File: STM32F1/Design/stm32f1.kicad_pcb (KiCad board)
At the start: 2 copper layers, 31 parts, among them J1 USB_C_Receptacle_USB2.0, J2 Conn_01x04_Pin, J3 Conn_01x04_Pin, J4 Conn_01x04_Pin, SW1 SW_SPDT, U1 STM32F103C8Tx, U2 AMS1117-3.3, Y1 16MHz

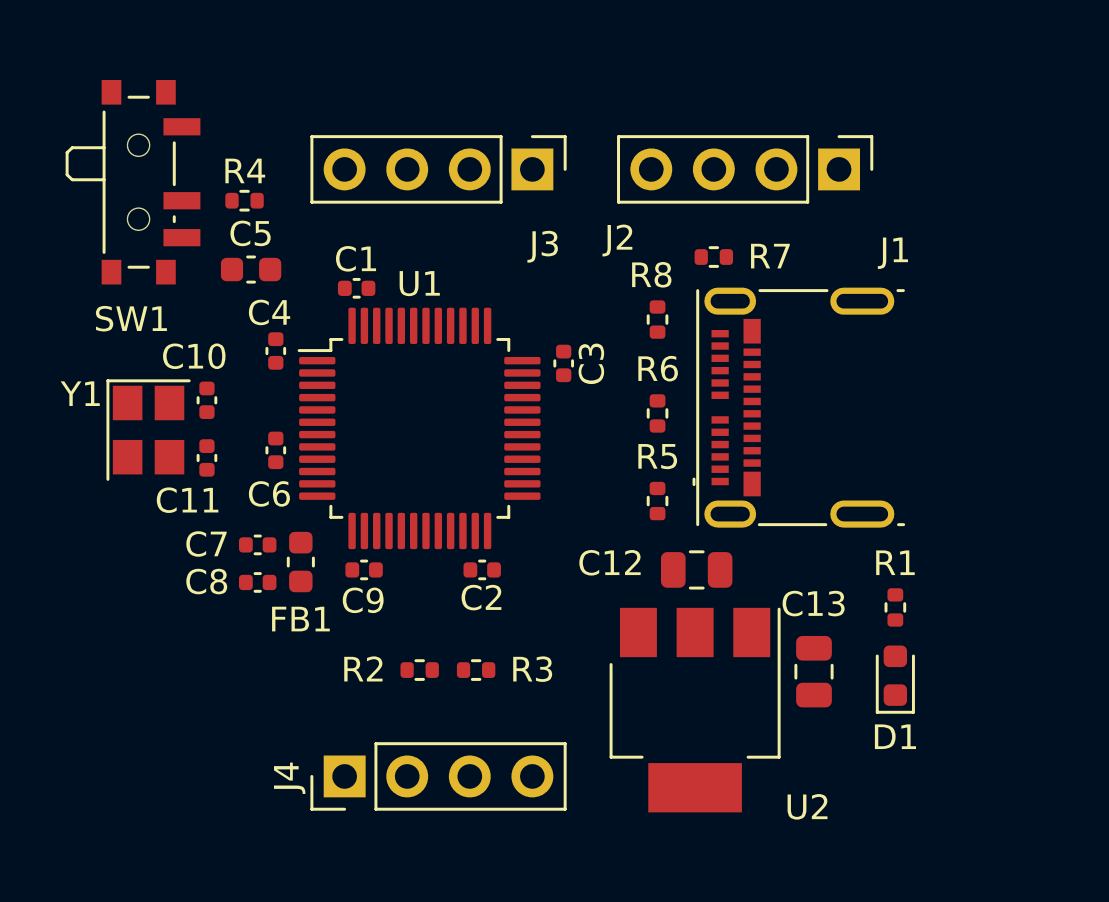
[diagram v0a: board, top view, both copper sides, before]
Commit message: Fine tunes PCB layout and added borders, Started routing
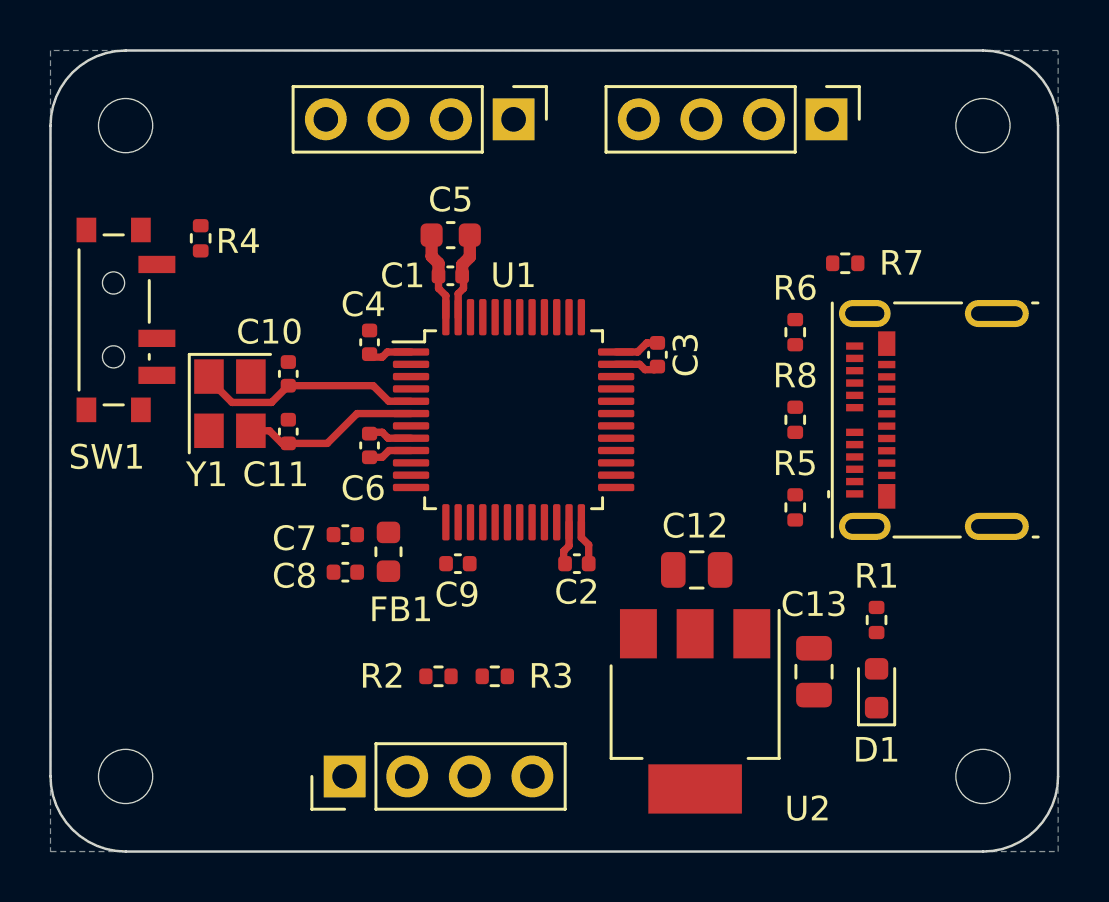
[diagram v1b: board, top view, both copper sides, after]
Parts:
- added H1: MountingHole, MountingHole:MountingHole_2.2mm_M2, F.Cu at (73.4, 55.4)
- added H2: MountingHole, MountingHole:MountingHole_2.2mm_M2, F.Cu at (73.4, 81.8)
- added H3: MountingHole, MountingHole:MountingHole_2.2mm_M2, F.Cu at (38.6, 55.4)
- added H4: MountingHole, MountingHole:MountingHole_2.2mm_M2, F.Cu at (38.6, 81.8)
- moved C5 8.22 mm to (51.8, 59.8)
- moved R8 6.91 mm to (65.8, 67.3), turned to -90 degrees
- moved R6 6.49 mm to (65.8, 63.8)
- moved SW1 5.68 mm to (38.4, 63.3)
- moved R5 5.59 mm to (65.8, 70.9)
- moved J1 5.49 mm to (71.4, 67.3)
- moved R7 5.34 mm to (67.8, 61.0)
- moved C2 3.85 mm to (56.9, 73.2)
- moved C1 3.84 mm to (51.8, 61.5)
- moved C3 3.82 mm to (60.2, 64.7)
- moved U1 3.82 mm to (54.4, 67.3)
- moved C4 3.82 mm to (48.5, 64.2)
- moved C9 3.81 mm to (52.1, 73.2)
- moved C6 3.81 mm to (48.5, 68.4)
- moved C7 3.58 mm to (47.5, 72.0)
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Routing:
- net /HSE_IN: track 0.00 -> 9.25 mm
- net +3.3V: track 0.00 -> 9.02 mm
- net GND: track 0.00 -> 8.97 mm
- net /HSE_OUT: track 0.00 -> 7.21 mm
- net +3.3VA: track 0.00 -> 1.80 mm
- added copper zone on B.Cu, net GND
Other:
- board outline added: 40.9 x 32.5 mm

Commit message: Completed Board design
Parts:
- J1: footprint Connector_USB:USB_C_Receptacle_Molex_105450-0101 -> Connector_USB:USB_C_Receptacle_HRO_TYPE-C-31-M-12
- moved R5 7.55 mm to (72.9, 73.4), turned to 0 degrees
- moved J1 0.94 mm to (72.4, 67.3)
- moved D1 0.93 mm to (70.0, 78.5), turned to -90 degrees
- moved R1 0.89 mm to (70.0, 75.4)
- moved C2 0.25 mm to (57.2, 73.2)
- turned C13 to 90 degrees
- turned C7 to 180 degrees
- turned C8 to 180 degrees
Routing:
- net +3.3V: track 9.02 -> 174.7 mm, vias 0 -> 11
- net GND: track 8.97 -> 47.6 mm, vias 0 -> 20
- net Net-(J1-SHIELD): track 0.00 -> 19.4 mm
- net VBUS: track 0.00 -> 17.8 mm
- net /BOOT0: track 0.00 -> 16.7 mm
- net /SWDIO: track 0.00 -> 14.3 mm
- net /USB_D+: track 0.00 -> 13.3 mm
- net /USB_D-: track 0.03 -> 12.7 mm
- net /I2C2_SCL: track 0.00 -> 12.6 mm
- net /USART1_RX: track 0.00 -> 12.2 mm
- net /I2C2_SDA: track 0.00 -> 11.8 mm
- net /USART1_TX: track 0.00 -> 10.5 mm
- net /SWCLK: track 0.00 -> 10.0 mm
- net Net-(J1-CC1): track 0.00 -> 8.86 mm, vias 0 -> 2
- net /NRST: track 0.00 -> 8.77 mm
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- added copper zone on F.Cu, net +3.3V
- added copper zone on F.Cu, net GND
- added copper zone on F.Cu, net VBUS
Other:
- board text added: "-"
- board text added: "BOOT"
- board text added: "I2C"
- board text added: "MAGNUS HADES"
- board text added: "SWD"
- board text added: "UART"
- board text added: "v1.0"

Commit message: Removed unwanted files
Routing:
- net GND: track 47.6 -> 47.0 mm
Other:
- board text added: "2023"
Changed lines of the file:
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@@
     (property "ki_keywords" "cap capacitor")
     (attr smd)
-    (fp_text reference "C10" (at 1.694 -0.762 180) (layer "F.SilkS")
+    (fp_text reference "C10" (at 1.694 0 180) (layer "F.SilkS")
         (effects (font (size 0.8 0.8) (thickness 0.15)))
     )
@@
   (gr_arc (start 73.406 52.324) (mid 75.561261 53.216739) (end 76.454 55.372)
     (stroke (width 0.1) (type default)) (layer "Edge.Cuts"))
-  (gr_text "v1.0" (at 37.338 76.708 90) (layer "B.SilkS")
+  (gr_text "2023" (at 37.338 75.946 90) (layer "B.SilkS")
+    (effects (font (size 0.85 0.85) (thickness 0.15)) (justify left bottom mirror))
+  )
+  (gr_text "v1.0" (at 37.338 72.39 90) (layer "B.SilkS")
     (effects (font (size 0.85 0.85) (thickness 0.15)) (justify left bottom mirror))
   )
@@
   (segment (start 44.958 56.896) (end 46.736 55.118) (width 0.5) (layer "F.Cu") (net 2))
   (segment (start 41.992 68.154) (end 42.926 69.088) (width 0.5) (layer "F.Cu") (net 2))
+  (segment (start 39.86 61.02) (end 40.386 60.494) (width 0.5) (layer "F.Cu") (net 2))
   (segment (start 52.106 63.986041) (end 51.857041 64.235) (width 0.3) (layer "F.Cu") (net 2))
-  (segment (start 40.386 60.5) (end 40.386 59.69) (width 0.3) (layer "F.Cu") (net 2))
   (segment (start 46.172 64.968) (end 46.228 65.024) (width 0.5) (layer "F.Cu") (net 2))
   (segment (start 52.106 63.1475) (end 52.106 62.194) (width 0.3) (layer "F.Cu") (net 2))
@@
   (segment (start 52.106 63.1475) (end 52.106 63.986041) (width 0.3) (layer "F.Cu") (net 2))
   (segment (start 56.606 70.14) (end 56.642 70.104) (width 0.3) (layer "F.Cu") (net 2))
-  (segment (start 43.692 65.558) (end 43.692 65.282) (width 0.5) (layer "F.Cu") (net 2))
+  (segment (start 40.386 60.494) (end 40.386 59.69) (width 0.5) (layer "F.Cu") (net 2))
   (segment (start 52.578 60.706) (end 52.578 59.817) (width 0.5) (layer "F.Cu") (net 2))
   (segment (start 67.11 64.062) (end 66.294 63.246) (width 0.5) (layer "F.Cu") (net 2))
+  (segment (start 43.692 64.012) (end 43.692 65.558) (width 0.5) (layer "F.Cu") (net 2))
   (segment (start 60.0675 65.278) (end 60.194 65.1515) (width 0.3) (layer "F.Cu") (net 2))
   (segment (start 70.991 74.928) (end 70.993 74.93) (width 0.5) (layer "F.Cu") (net 2))
@@
   (segment (start 47.046 73.4975) (end 47.046 74.366) (width 0.5) (layer "F.Cu") (net 2))
   (segment (start 60.194 65.1515) (end 61.0875 65.1515) (width 0.5) (layer "F.Cu") (net 2))
+  (segment (start 43.688 64.008) (end 43.692 64.012) (width 0.5) (layer "F.Cu") (net 2))
   (segment (start 58.5185 65.06) (end 59.472 65.06) (width 0.3) (layer "F.Cu") (net 2))
   (segment (start 47.046 70.922) (end 46.99 70.866) (width 0.5) (layer "F.Cu") (net 2))
   (segment (start 65.786 63.246) (end 65.786 62.23) (width 0.5) (layer "F.Cu") (net 2))
-  (segment (start 39.878 61.008) (end 40.386 60.5) (width 0.3) (layer "F.Cu") (net 2))
   (segment (start 66.548 70.612) (end 66.598 70.562) (width 0.5) (layer "F.Cu") (net 2))
   (segment (start 40.386 58.928) (end 42.418 56.896) (width 0.5) (layer "F.Cu") (net 2))
   (segment (start 47.046 71.9735) (end 47.046 70.922) (width 0.5) (layer "F.Cu") (net 2))
   (segment (start 68.311 64.062) (end 67.11 64.062) (width 0.5) (layer "F.Cu") (net 2))
-  (segment (start 43.692 65.282) (end 42.418 64.008) (width 0.5) (layer "F.Cu") (net 2))
   (segment (start 66.294 63.246) (end 65.786 63.246) (width 0.5) (layer "F.Cu") (net 2))
   (segment (start 52.268 61.016) (end 52.578 60.706) (width 0.5) (layer "F.Cu") (net 2))
@@
   (via (at 53.594 73.152) (size 0.8) (drill 0.4) (layers "F.Cu" "B.Cu") (net 2))
   (via (at 46.228 67.31) (size 0.8) (drill 0.4) (layers "F.Cu" "B.Cu") (net 2))
-  (via (at 42.418 64.008) (size 0.7) (drill 0.3) (layers "F.Cu" "B.Cu") (net 2))
+  (via (at 43.688 64.008) (size 0.7) (drill 0.3) (layers "F.Cu" "B.Cu") (net 2))
   (via (at 51.689 68.072) (size 0.8) (drill 0.4) (layers "F.Cu" "B.Cu") (net 2))
   (via (at 64.262 73.914) (size 0.7) (drill 0.3) (layers "F.Cu" "B.Cu") (net 2))
